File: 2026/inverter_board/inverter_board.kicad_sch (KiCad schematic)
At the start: 36 parts, among them J1 RJ12, J2 RJ12, J3 Modbus, J4 PROG, U1 CH32V003JxMx, U2 HCPL-0611, U3 HCPL-0611, U4 HCPL-0611, U5 MAX485E, U6 ME6209A50M3G

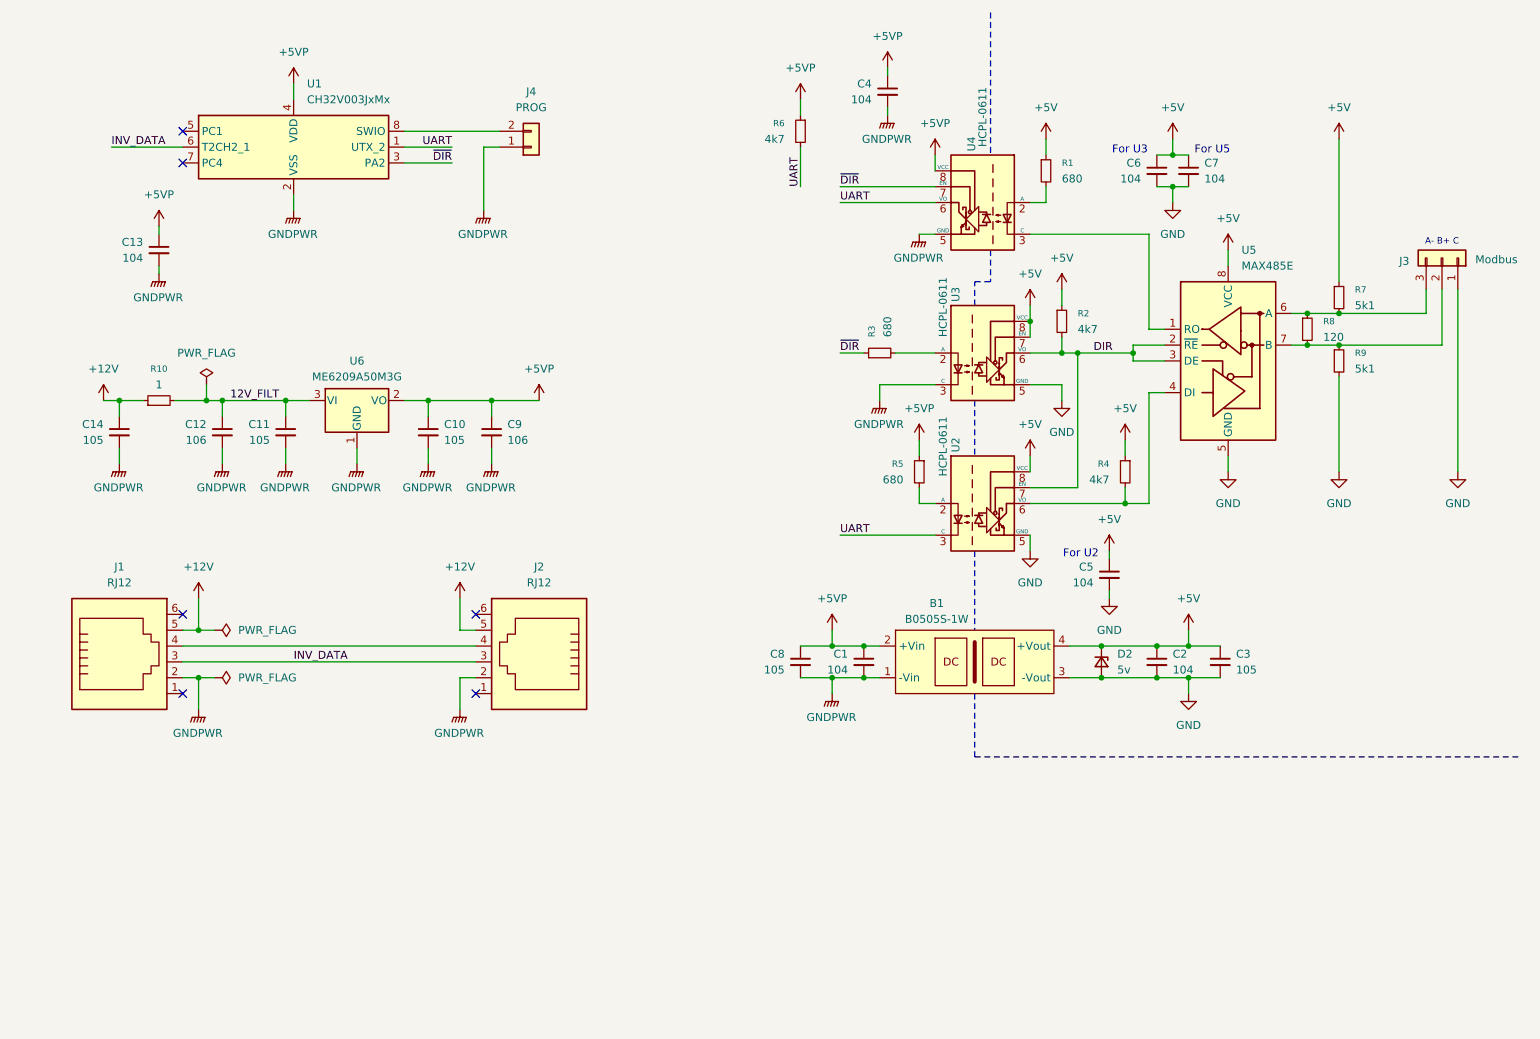
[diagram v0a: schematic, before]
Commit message: Updated inverter decoder board to use a buck converter
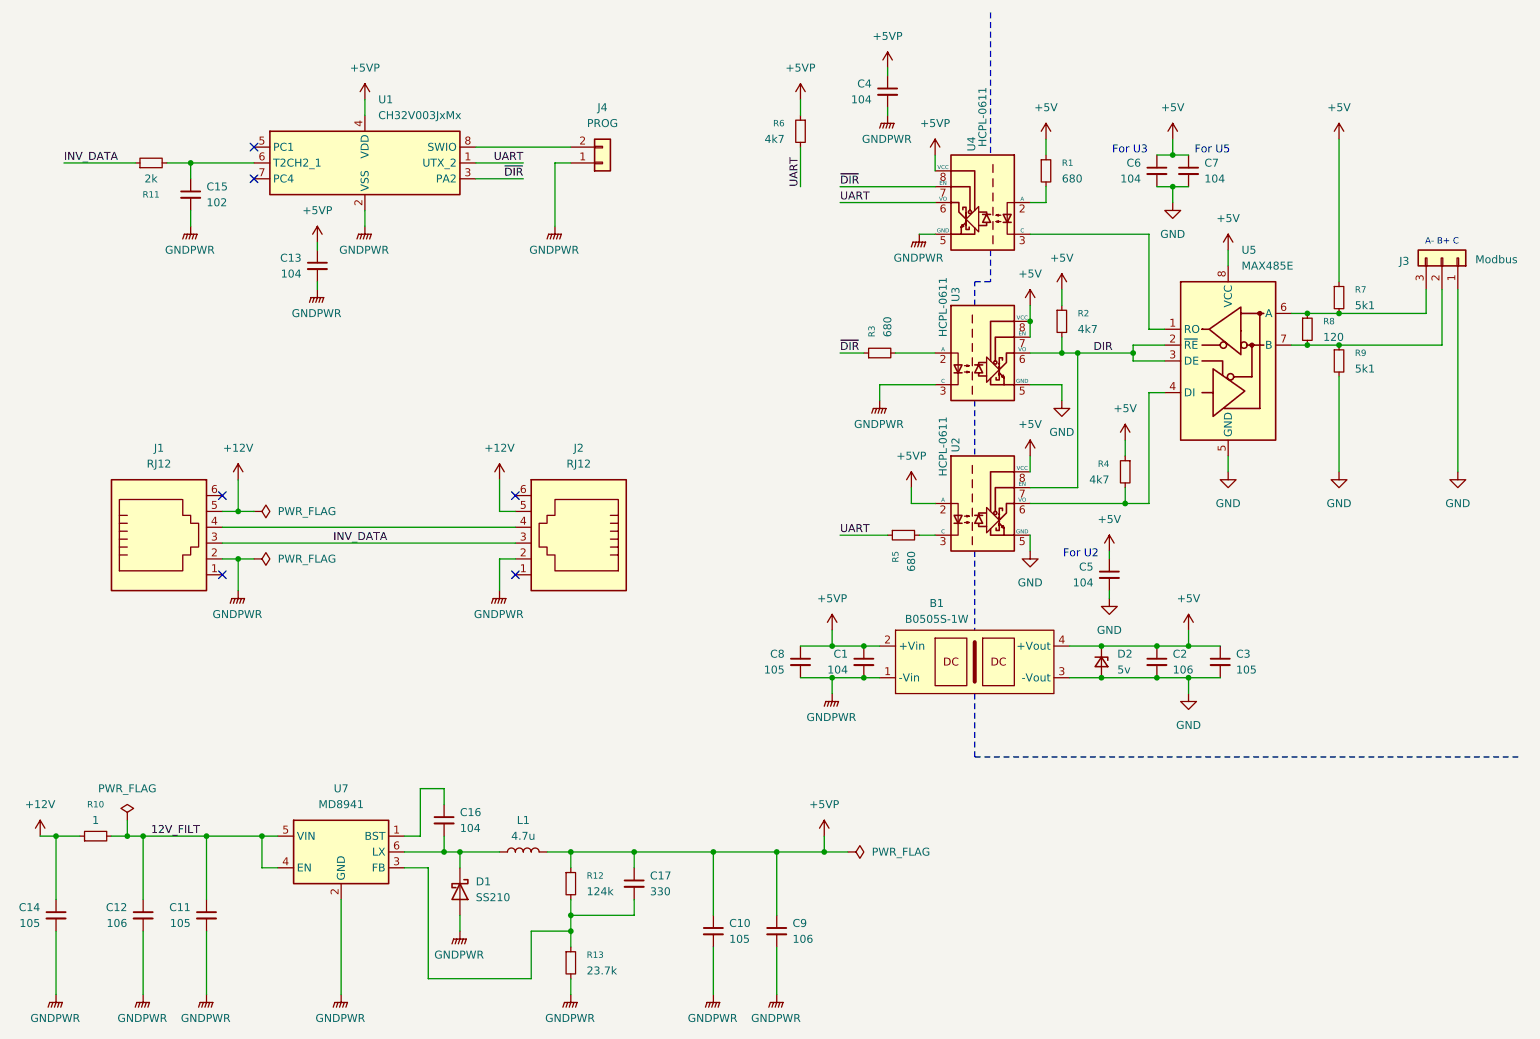
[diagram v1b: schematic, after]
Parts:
- removed U6: ME6209A50M3G, Package_TO_SOT_SMD:SOT-23, symbol Regulator_Linear:APE8865N-12-HF-3
- added C15: 102, Capacitor_SMD:C_0603_1608Metric, symbol Device:C_Small
- added C16: 104, Capacitor_SMD:C_0603_1608Metric, symbol Device:C_Small
- added C17: 330, Capacitor_SMD:C_0603_1608Metric, symbol Device:C_Small
- added D1: SS210, Diode_SMD:D_SMA, symbol Diode:SS210
- added L1: 4.7u, Inductor_SMD:L_APV_APH0420, symbol Device:L
- added R11: 2k, Resistor_SMD:R_0603_1608Metric, symbol Device:R_Small
- added R12: 124k, Resistor_SMD:R_0603_1608Metric, symbol Device:R_Small
- added R13: 23.7k, Resistor_SMD:R_0603_1608Metric, symbol Device:R_Small
- added U7: MD8941, Package_TO_SOT_SMD:SOT-23-6, symbol Regulator_Switching:AOZ1282CI-1
- C2: value 104 -> 106; footprint Capacitor_SMD:C_0603_1608Metric -> Capacitor_SMD:C_1206_3216Metric
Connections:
- net +5VP: now also U2.2 (A), C17.1, L1.2, R12.1; no longer R5.1
- net 12V_FILT: now also U7.4 (EN), U7.5 (VIN)
- net GNDPWR: now also C15.2, D1.2 (A), R13.2, U7.2 (GND)
- net INV_DATA: now also R11.1; no longer U1.6 (PC2)
- net UART: now also R5.1; no longer U2.3 (C)
- net at R5.2: now also U2.3 (C); no longer U2.2 (A)
- new net: C16.1, U7.1 (BST)
- new net: C17.2, R12.2, R13.1, U7.3 (FB)
- new net: C16.2, D1.1 (K), L1.1, U7.6 (LX)
- new net: C15.1, R11.2, U1.6 (PC2)
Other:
- moved on the sheet: C10, C11, C12, C13, C14, C9, J1, J2, J4, R10, R5, U1
